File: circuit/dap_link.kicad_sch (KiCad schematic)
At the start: 29 parts, among them J1 USB_A_CONN, J2 SWD_CONN_5P, J3 UART1_CONN_3P, J5 Conn_02x10_Odd_Even, U1 STM32F103CBTx, U2 AMS1117-3.3, U3 TXS0108EPW, Y1 8MHz

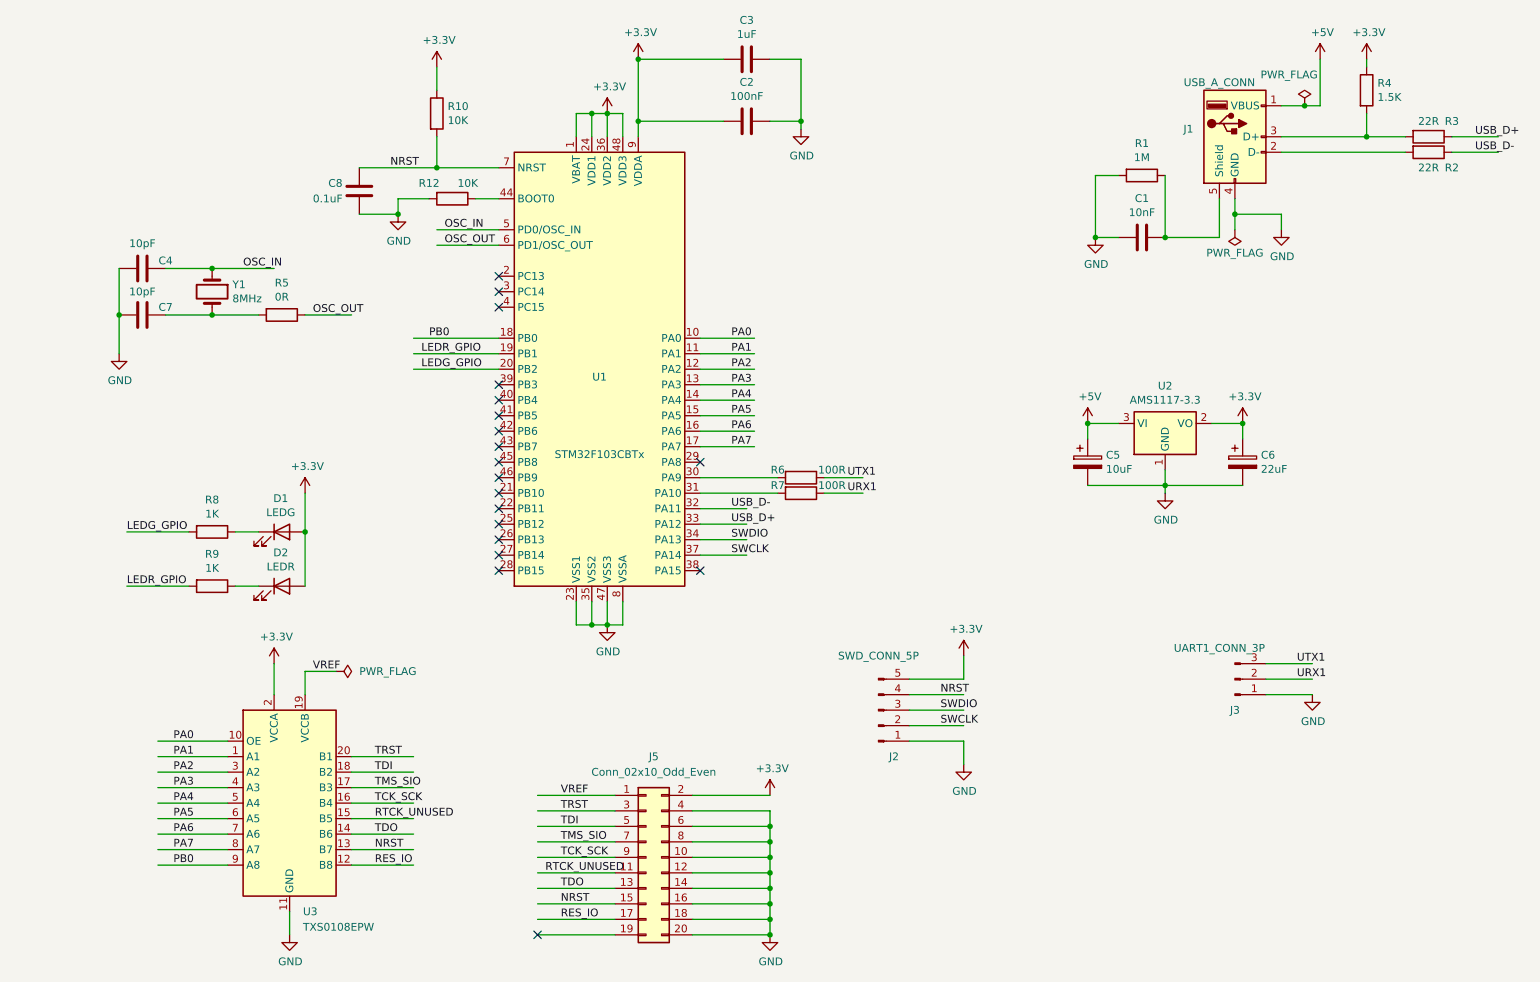
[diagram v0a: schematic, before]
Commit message: kicad有DRC错误
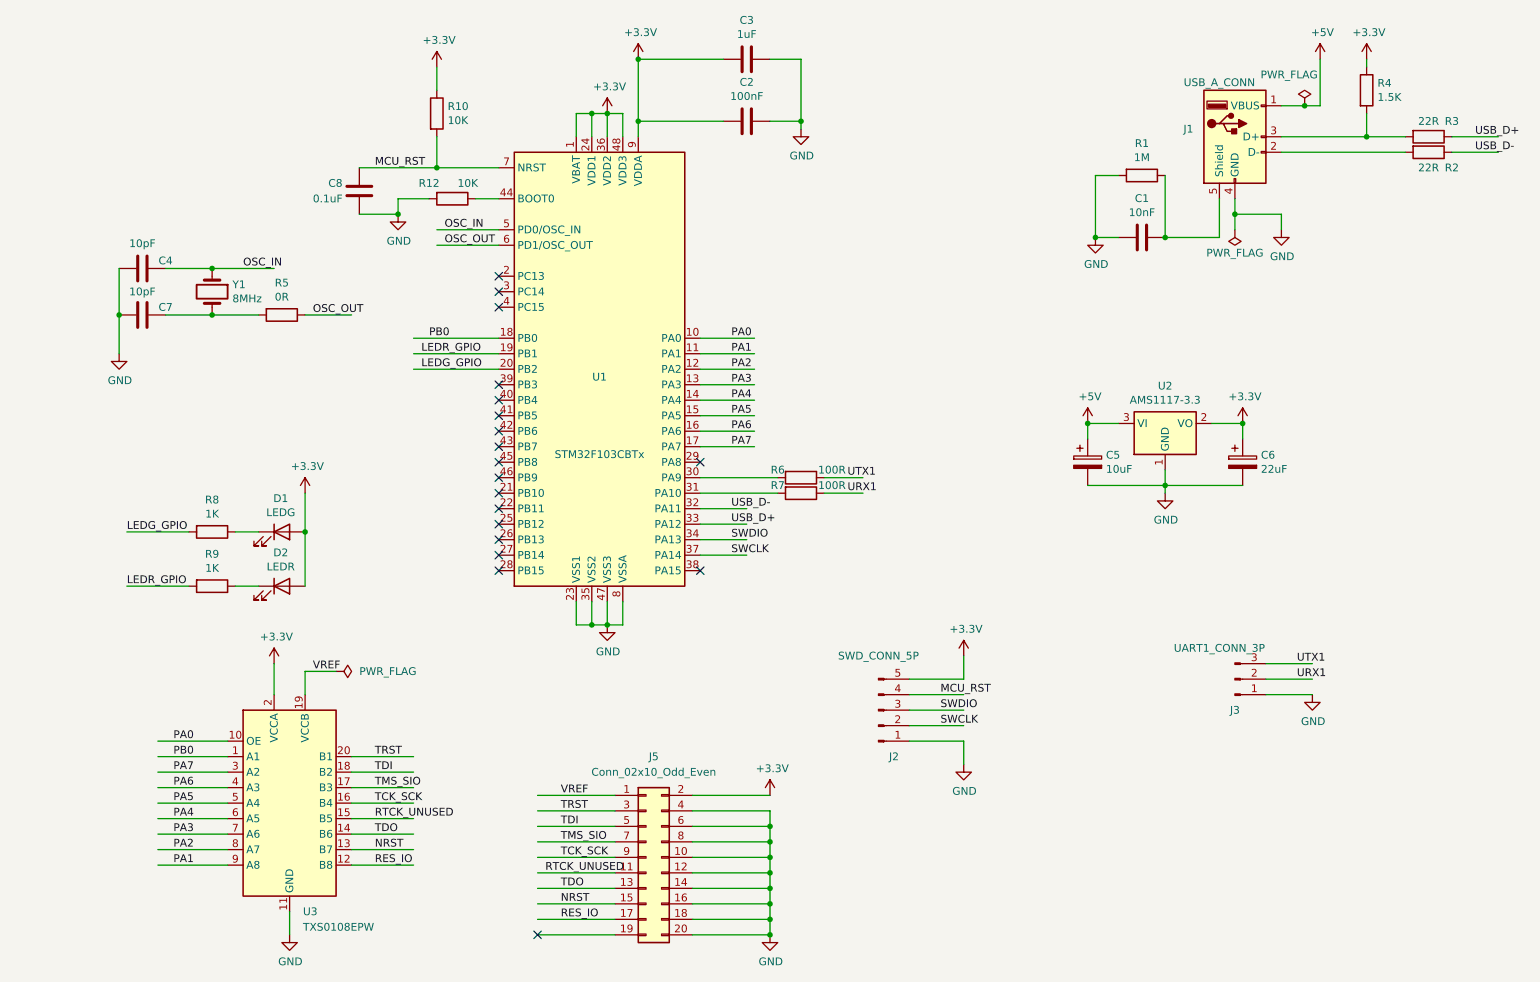
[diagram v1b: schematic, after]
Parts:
- D1, D2: footprint LED_SMD:LED_0603_1608Metric_Pad1.05x0.95mm_HandSolder -> Diode_SMD:D_0805_2012Metric_Pad1.15x1.40mm_HandSolder
- J5: footprint Connector_PinSocket_2.54mm:PinSocket_2x10_P2.54mm_Horizontal -> Connector_PinSocket_2.54mm:PinSocket_2x10_P2.54mm_Vertical
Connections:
- net NRST: no longer C8.1, J2.4 (Pin_4), R10.2, U1.7 (NRST)
- net PA1: now also U3.9 (A8); no longer U3.1 (A1)
- net PA2: now also U3.8 (A7); no longer U3.3 (A2)
- net PA3: now also U3.7 (A6); no longer U3.4 (A3)
- net PA4: now also U3.6 (A5); no longer U3.5 (A4)
- net PA5: now also U3.5 (A4); no longer U3.6 (A5)
- net PA6: now also U3.4 (A3); no longer U3.7 (A6)
- net PA7: now also U3.3 (A2); no longer U3.8 (A7)
- net PB0: now also U3.1 (A1); no longer U3.9 (A8)
- new net MCU_RST: C8.1, J2.4 (Pin_4), R10.2, U1.7 (NRST)
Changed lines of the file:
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@@
     (stroke (width 0) (type default))
   )
-  (label "NRST" (at 167.64 138.43 0) (fields_autoplaced)
+  (label "MCU_RST" (at 167.64 138.43 0) (fields_autoplaced)
     (effects (font (size 1.27 1.27)) (justify left bottom))
   )
@@
     (effects (font (size 1.27 1.27)) (justify left bottom))
   )
+  (label "PA6" (at 41.91 153.67 0) (fields_autoplaced)
+    (effects (font (size 1.27 1.27)) (justify left bottom))
+  )
   (label "USB_D+" (at 133.35 110.49 0) (fields_autoplaced)
     (effects (font (size 1.27 1.27)) (justify left bottom))
@@
     (effects (font (size 1.27 1.27)) (justify left bottom))
   )
-  (label "NRST" (at 77.47 52.07 0) (fields_autoplaced)
+  (label "PA1" (at 41.91 166.37 0) (fields_autoplaced)
     (effects (font (size 1.27 1.27)) (justify left bottom))
   )
@@
     (effects (font (size 1.27 1.27)) (justify left bottom))
   )
-  (label "PB0" (at 41.91 166.37 0) (fields_autoplaced)
-    (effects (font (size 1.27 1.27)) (justify left bottom))
-  )
   (label "PA2" (at 133.35 85.09 0) (fields_autoplaced)
     (effects (font (size 1.27 1.27)) (justify left bottom))
   )
-  (label "PA7" (at 41.91 163.83 0) (fields_autoplaced)
-    (effects (font (size 1.27 1.27)) (justify left bottom))
-  )
   (label "SWCLK" (at 167.64 143.51 0) (fields_autoplaced)
     (effects (font (size 1.27 1.27)) (justify left bottom))
@@
     (effects (font (size 1.27 1.27)) (justify left bottom))
   )
-  (label "PA6" (at 41.91 161.29 0) (fields_autoplaced)
-    (effects (font (size 1.27 1.27)) (justify left bottom))
-  )
-  (label "PA5" (at 41.91 158.75 0) (fields_autoplaced)
-    (effects (font (size 1.27 1.27)) (justify left bottom))
-  )
   (label "PA7" (at 133.35 97.79 0) (fields_autoplaced)
     (effects (font (size 1.27 1.27)) (justify left bottom))
   )
-  (label "PA4" (at 41.91 156.21 0) (fields_autoplaced)
-    (effects (font (size 1.27 1.27)) (justify left bottom))
-  )
   (label "OSC_OUT" (at 86.36 64.77 0) (fields_autoplaced)
     (effects (font (size 1.27 1.27)) (justify left bottom))
   )
+  (label "PA5" (at 41.91 156.21 0) (fields_autoplaced)
+    (effects (font (size 1.27 1.27)) (justify left bottom))
+  )
   (label "LEDR_GPIO" (at 34.29 120.65 0) (fields_autoplaced)
     (effects (font (size 1.27 1.27)) (justify left bottom))
@@
     (effects (font (size 1.27 1.27)) (justify left bottom))
   )
-  (label "PA2" (at 41.91 151.13 0) (fields_autoplaced)
-    (effects (font (size 1.27 1.27)) (justify left bottom))
-  )
   (label "TDO" (at 105.41 170.18 0) (fields_autoplaced)
     (effects (font (size 1.27 1.27)) (justify left bottom))
   )
+  (label "PA4" (at 41.91 158.75 0) (fields_autoplaced)
+    (effects (font (size 1.27 1.27)) (justify left bottom))
+  )
   (label "UTX1" (at 226.06 133.35 0) (fields_autoplaced)
     (effects (font (size 1.27 1.27)) (justify left bottom))
@@
     (effects (font (size 1.27 1.27)) (justify left bottom))
   )
+  (label "PB0" (at 41.91 148.59 0) (fields_autoplaced)
+    (effects (font (size 1.27 1.27)) (justify left bottom))
+  )
+  (label "MCU_RST" (at 74.93 52.07 0) (fields_autoplaced)
+    (effects (font (size 1.27 1.27)) (justify left bottom))
+  )
   (label "RES_IO" (at 74.93 166.37 0) (fields_autoplaced)
     (effects (font (size 1.27 1.27)) (justify left bottom))
@@
     (effects (font (size 1.27 1.27)) (justify left bottom))
   )
+  (label "PA7" (at 41.91 151.13 0) (fields_autoplaced)
+    (effects (font (size 1.27 1.27)) (justify left bottom))
+  )
   (label "PA3" (at 133.35 87.63 0) (fields_autoplaced)
     (effects (font (size 1.27 1.27)) (justify left bottom))
@@
     (effects (font (size 1.27 1.27)) (justify left bottom))
   )
-  (label "PA1" (at 41.91 148.59 0) (fields_autoplaced)
-    (effects (font (size 1.27 1.27)) (justify left bottom))
-  )
   (label "TCK_SCK" (at 105.41 165.1 0) (fields_autoplaced)
     (effects (font (size 1.27 1.27)) (justify left bottom))
@@
     (effects (font (size 1.27 1.27)) (justify left bottom))
   )
-  (label "PA3" (at 41.91 153.67 0) (fields_autoplaced)
-    (effects (font (size 1.27 1.27)) (justify left bottom))
-  )
   (label "OSC_IN" (at 53.34 68.58 0) (fields_autoplaced)
     (effects (font (size 1.27 1.27)) (justify left bottom))
@@
     (effects (font (size 1.27 1.27)) (justify left bottom))
   )
+  (label "PA3" (at 41.91 161.29 0) (fields_autoplaced)
+    (effects (font (size 1.27 1.27)) (justify left bottom))
+  )
   (label "USB_D+" (at 255.27 46.99 0) (fields_autoplaced)
     (effects (font (size 1.27 1.27)) (justify left bottom))
@@
   )
   (label "NRST" (at 105.41 172.72 0) (fields_autoplaced)
+    (effects (font (size 1.27 1.27)) (justify left bottom))
+  )
+  (label "PA2" (at 41.91 163.83 0) (fields_autoplaced)
     (effects (font (size 1.27 1.27)) (justify left bottom))
   )
@@
       (effects (font (size 1.27 1.27)))
     )
-    (property "Footprint" "LED_SMD:LED_0603_1608Metric_Pad1.05x0.95mm_HandSolder" (at 59.69 111.76 0)
+    (property "Footprint" "Diode_SMD:D_0805_2012Metric_Pad1.15x1.40mm_HandSolder" (at 59.69 111.76 0)
       (effects (font (size 1.27 1.27)) hide)
     )
@@
       (effects (font (size 1.27 1.27)))
     )
-    (property "Footprint" "LED_SMD:LED_0603_1608Metric_Pad1.05x0.95mm_HandSolder" (at 59.69 120.65 0)
+    (property "Footprint" "Diode_SMD:D_0805_2012Metric_Pad1.15x1.40mm_HandSolder" (at 59.69 120.65 0)
       (effects (font (size 1.27 1.27)) hide)
     )
@@
       (effects (font (size 1.27 1.27)))
     )
-    (property "Footprint" "Connector_PinSocket_2.54mm:PinSocket_2x10_P2.54mm_Horizontal" (at 119.38 165.1 0)
-      (effects (font (size 1.27 1.27)) hide)
-    )
+    (property "Footprint" "Connector_PinSocket_2.54mm:PinSocket_2x10_P2.54mm_Vertical" (at 119.38 165.1 0)
+      (effects (font (size 1.27 1.27)) hide)
+    )

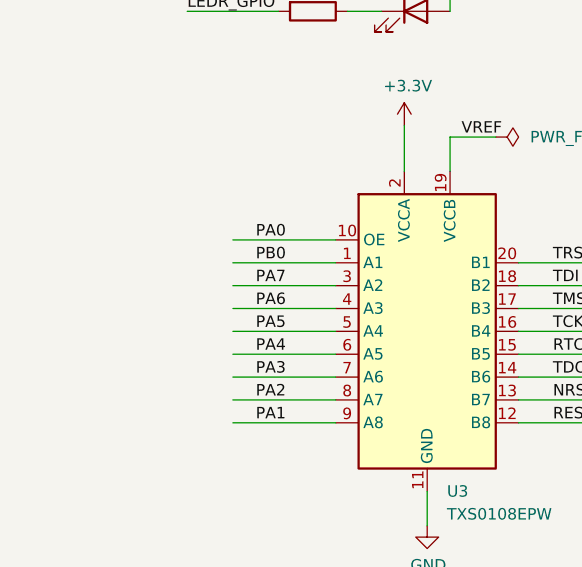
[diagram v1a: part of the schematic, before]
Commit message: 板子加OE下拉 IO初始化修改
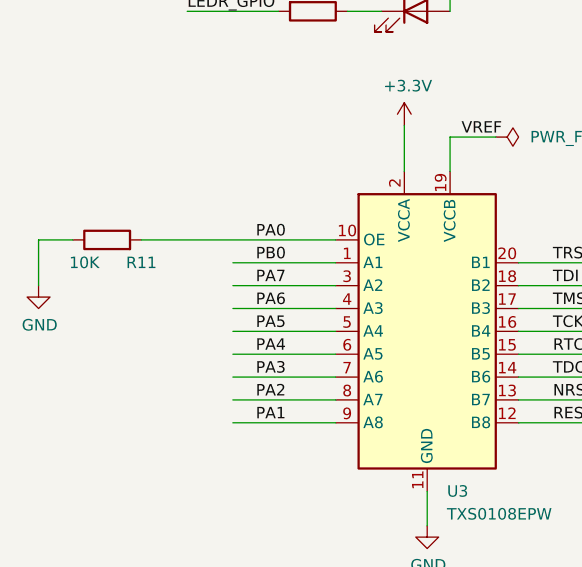
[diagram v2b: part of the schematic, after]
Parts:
- added R11: 10K, Resistor_SMD:R_0805_2012Metric_Pad1.20x1.40mm_HandSolder, symbol Device:R
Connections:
- net GND: now also R11.1
- net PA0: now also R11.2
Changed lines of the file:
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@@
     (stroke (width 0) (type default))
   )
-  (wire (pts (xy 39.37 146.05) (xy 50.8 146.05))
+  (wire (pts (xy 29.21 146.05) (xy 50.8 146.05))
     (stroke (width 0) (type default))
   )
@@
     (stroke (width 0) (type default))
   )
+  (wire (pts (xy 21.59 146.05) (xy 17.78 146.05))
+    (stroke (width 0) (type default))
+  )
   (wire (pts (xy 237.49 46.99) (xy 243.84 46.99))
     (stroke (width 0) (type default))
@@
   )
   (wire (pts (xy 162.56 138.43) (xy 171.45 138.43))
+    (stroke (width 0) (type default))
+  )
+  (wire (pts (xy 17.78 146.05) (xy 17.78 151.13))
     (stroke (width 0) (type default))
   )
@@
         )
       )
+    )
+  )
+  (symbol (lib_id "power:GND") (at 17.78 151.13 0) (unit 1)
+    (in_bom yes) (on_board yes) (dnp no)
+    (property "Reference" "#PWR020" (at 17.78 157.48 0)
+      (effects (font (size 1.27 1.27)) hide)
+    )
+    (property "Value" "GND" (at 17.907 155.5242 0)
+      (effects (font (size 1.27 1.27)))
+    )
+    (property "Footprint" "" (at 17.78 151.13 0)
+      (effects (font (size 1.27 1.27)) hide)
+    )
+    (property "Datasheet" "" (at 17.78 151.13 0)
+      (effects (font (size 1.27 1.27)) hide)
+    )
+    (pin "1")
+    (instances
+      (project "dap_link"
+        (path "/9df731a6-2e06-41f7-94bb-21385ffe9471"
+          (reference "#PWR020") (unit 1)
+        )
+      )
+    )
+  )
+  (symbol (lib_id "Device:R") (at 25.4 146.05 90) (unit 1)
+    (in_bom yes) (on_board yes) (dnp no)
+    (property "Reference" "R11" (at 29.21 148.59 90)
+      (effects (font (size 1.27 1.27)))
+    )
+    (property "Value" "10K" (at 22.86 148.59 90)
+      (effects (font (size 1.27 1.27)))
+    )
+    (property "Footprint" "Resistor_SMD:R_0805_2012Metric_Pad1.20x1.40mm_HandSolder" (at 25.4 147.828 90)
+      (effects (font (size 1.27 1.27)) hide)
+    )
+    (property "Datasheet" "~" (at 25.4 146.05 0)
+      (effects (font (size 1.27 1.27)) hide)
+    )
+    (pin "1")
+    (pin "2")
+    (instances
+      (project "dap_link"
+        (path "/9df731a6-2e06-41f7-94bb-21385ffe9471"
+          (reference "R11") (unit 1)
+        )
+      )

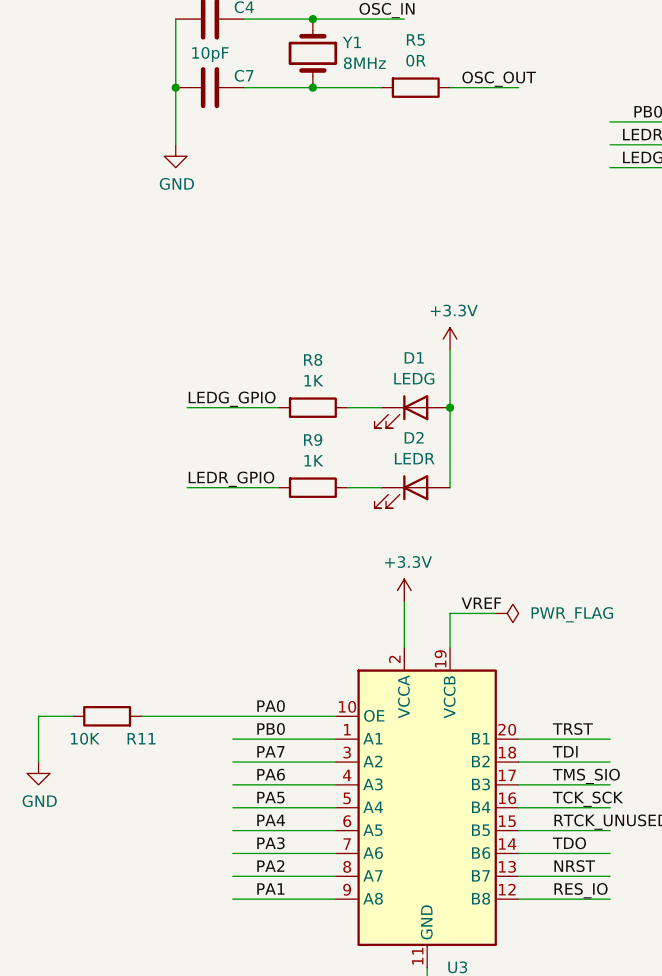
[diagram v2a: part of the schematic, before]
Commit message: 增加电源指示灯
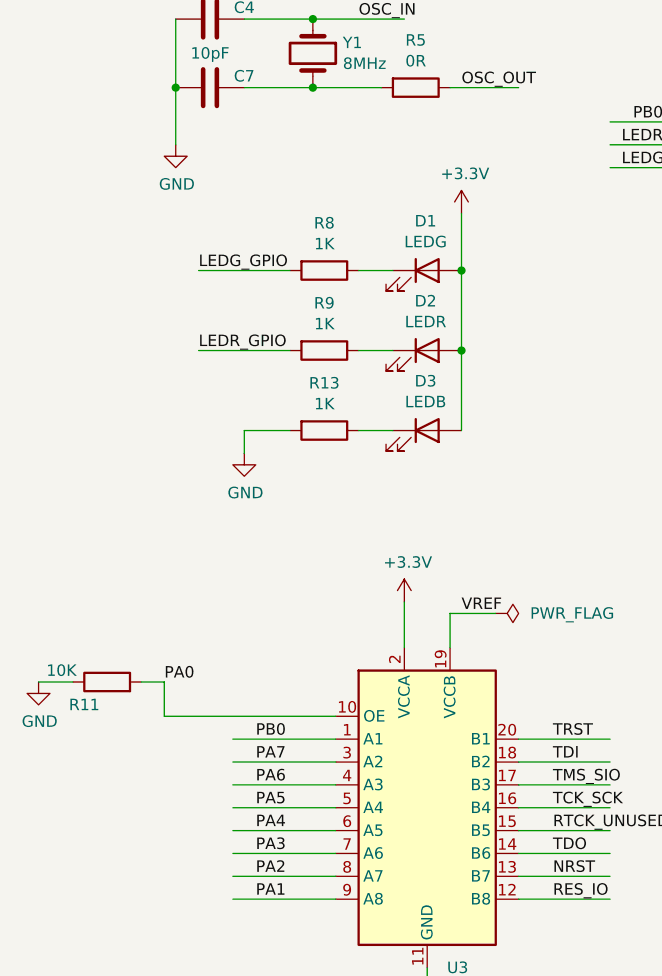
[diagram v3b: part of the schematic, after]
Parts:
- added D3: LEDB, Diode_SMD:D_0805_2012Metric_Pad1.15x1.40mm_HandSolder, symbol Device:LED
- added R13: 1K, Resistor_SMD:R_0805_2012Metric_Pad1.20x1.40mm_HandSolder, symbol Device:R
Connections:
- net +3V3: now also D3.2 (A)
- net GND: now also R13.2
- new net: D3.1 (K), R13.1
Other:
- moved on the sheet: D1, D2, R11, R8, R9

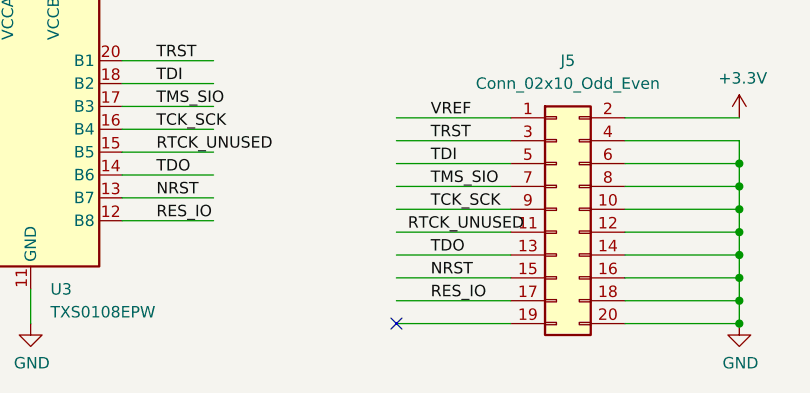
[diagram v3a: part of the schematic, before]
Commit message: 接口增加一个3.3V
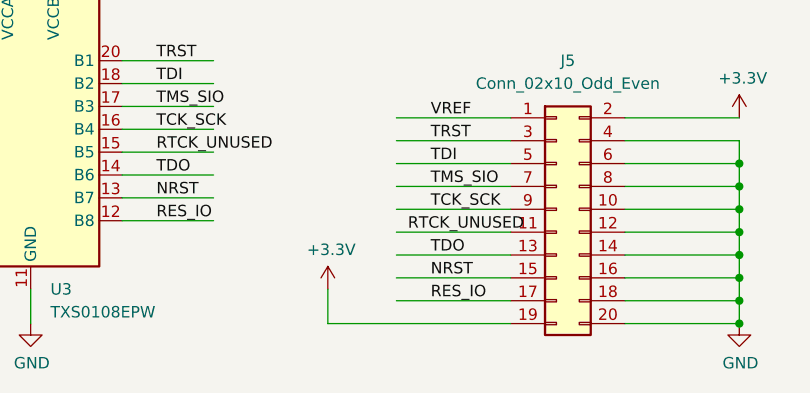
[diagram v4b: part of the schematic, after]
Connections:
- net +3V3: now also J5.19 (Pin_19)
- no-connect marks 19 -> 18
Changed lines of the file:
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@@
   (no_connect (at 95.25 97.79))
   (no_connect (at 95.25 95.25))
-  (no_connect (at 101.6 177.8))
   (no_connect (at 95.25 100.33))
   (no_connect (at 95.25 102.87))
@@
     (stroke (width 0) (type default))
   )
-  (wire (pts (xy 101.6 177.8) (xy 114.3 177.8))
+  (wire (pts (xy 93.98 177.8) (xy 114.3 177.8))
     (stroke (width 0) (type default))
   )
@@
   )
   (wire (pts (xy 107.95 43.18) (xy 110.49 43.18))
+    (stroke (width 0) (type default))
+  )
+  (wire (pts (xy 93.98 173.99) (xy 93.98 177.8))
     (stroke (width 0) (type default))
   )
@@
         )
       )
+    )
+  )
+  (symbol (lib_id "dap_link-rescue:+3.3V-power") (at 93.98 173.99 0) (unit 1)
+    (in_bom yes) (on_board yes) (dnp no)
+    (property "Reference" "#PWR022" (at 93.98 177.8 0)
+      (effects (font (size 1.27 1.27)) hide)
+    )
+    (property "Value" "+3.3V" (at 94.361 169.5958 0)
+      (effects (font (size 1.27 1.27)))
+    )
+    (property "Footprint" "" (at 93.98 173.99 0)
+      (effects (font (size 1.27 1.27)) hide)
+    )
+    (property "Datasheet" "" (at 93.98 173.99 0)
+      (effects (font (size 1.27 1.27)) hide)
+    )
+    (pin "1")
+    (instances
+      (project "dap_link"
+        (path "/9df731a6-2e06-41f7-94bb-21385ffe9471"
+          (reference "#PWR022") (unit 1)
+        )
+      )
